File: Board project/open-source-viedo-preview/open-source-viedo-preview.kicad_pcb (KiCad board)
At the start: 4 copper layers, 99.6 x 55.4 mm, 98 parts, among them J1 Conn_02x07_Odd_Even, J10 Conn_01x22_Female, J11 HDMI_A_1.4, J12 HDMI_A_1.4, J13 Screw_Terminal_01x02, J14 AMP171826-4, J15 10018783-11200TLF, J16 USB_OTG, J2 Conn_01x03, J3 Conn_01x03, J4 7499110124, J5 Micro_SD_Card_Det, J6 Conn_02x20_Odd_Even, J7 Conn_01x22_Female, J8 Conn_01x22_Female, J9 Conn_01x22_Female, Q1 DMP3013SFV-7, Q2 BSS138PW, U1 74LVC1G07, U131 TPD4EUSB30, U132 TPD4EUSB30, U2 74LVC1G07, U3 AP64501SP-13, U4 AP64501SP-13, U5 TPD2E009DBZR, U6 TPD2E009DBZR

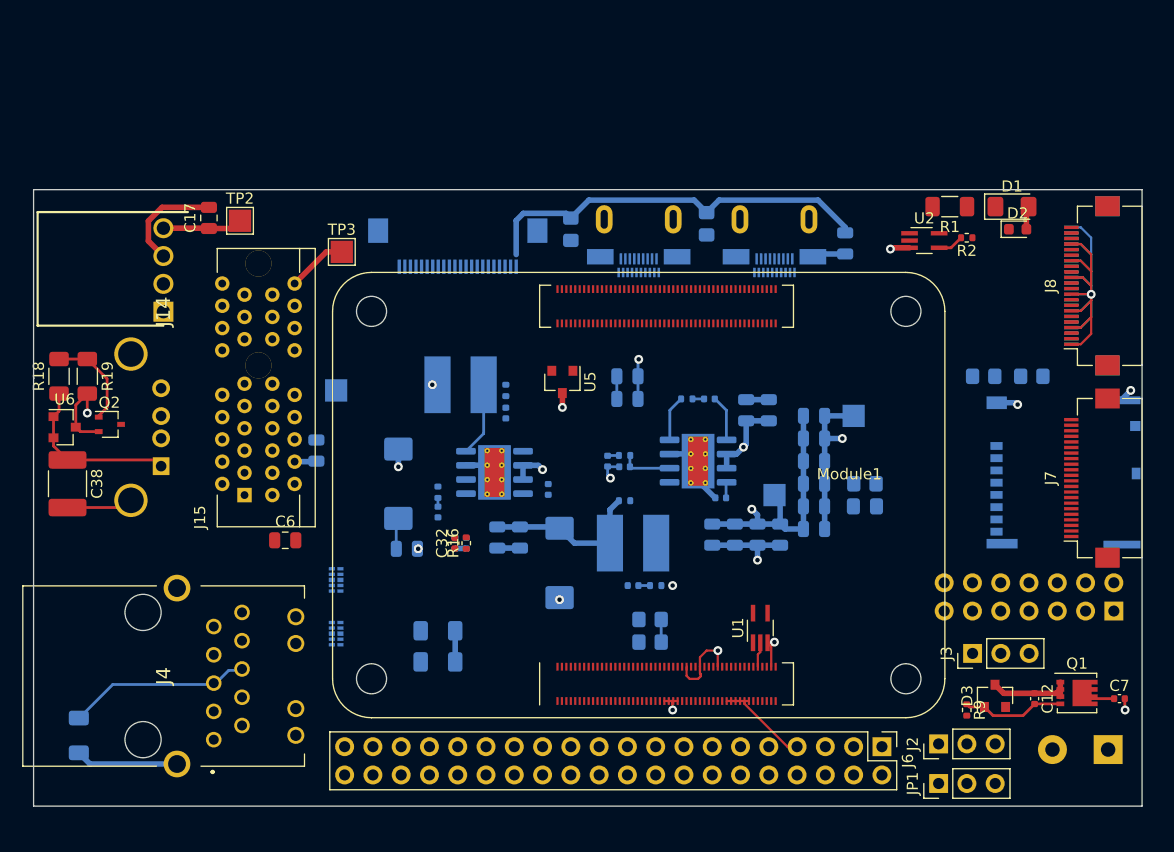
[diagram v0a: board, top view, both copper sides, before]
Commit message: Elements new placement
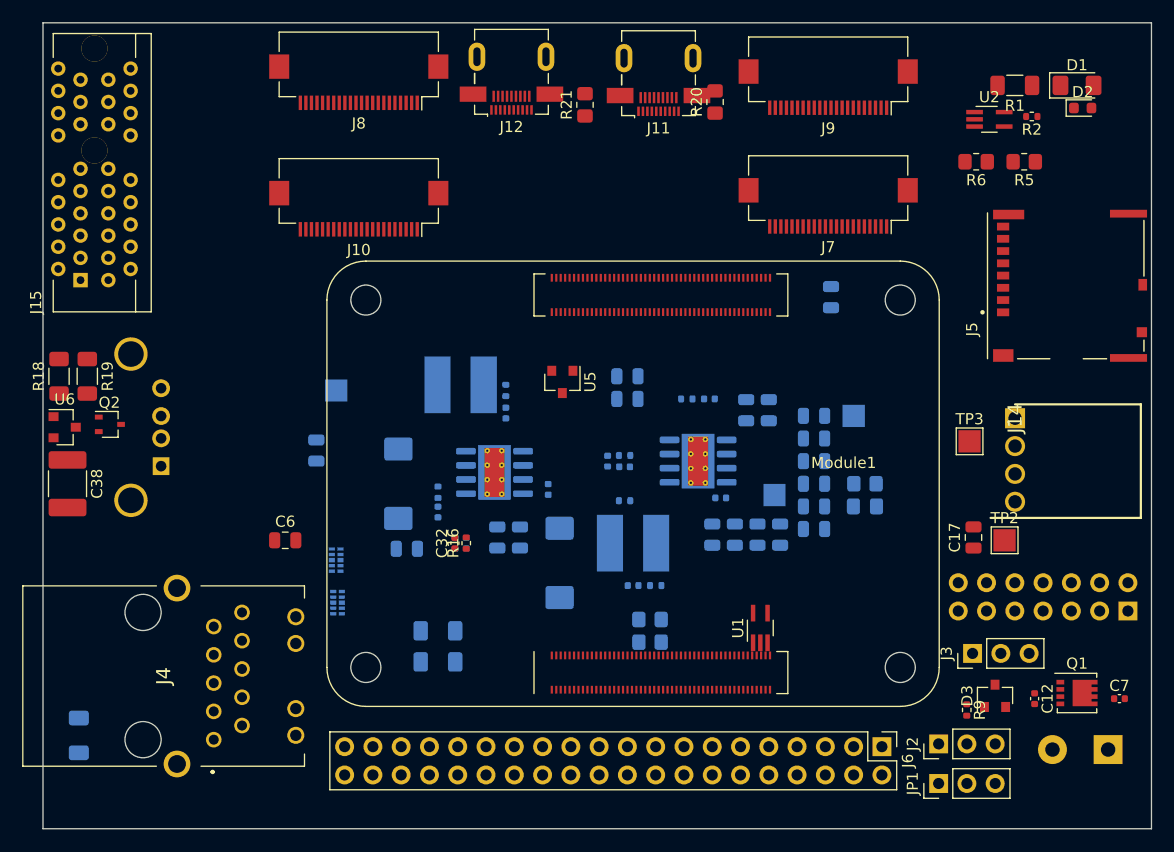
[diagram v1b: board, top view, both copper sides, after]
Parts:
- J10, J11, J12, J5, J9, R20, R21, R5, R6: moved to F.Cu
- moved J14 77.1 mm to (189.8, 55.1), turned to -90 degrees
- moved C17 74.4 mm to (186.0, 65.8)
- moved TP2 74.4 mm to (188.8, 66.0)
- moved J8 68.3 mm to (130.8, 24.9), turned to 180 degrees
- moved TP3 58.9 mm to (185.7, 57.1)
- moved J7 34.0 mm to (173.0, 36.0), turned to 180 degrees
- moved J9 29.7 mm to (173.0, 25.3), turned to 180 degrees
- moved J12 27.8 mm to (144.5, 22.6), turned to 180 degrees
- moved J15 24.3 mm to (105.8, 42.7)
- moved R6 19.9 mm to (186.3, 32.0), turned to 180 degrees
- moved R5 19.6 mm to (190.6, 32.0), turned to 180 degrees
- moved R20 17.3 mm to (162.8, 26.7), turned to 90 degrees
- moved J5 16.8 mm to (194.3, 43.2), turned to 90 degrees
- moved R21 15.3 mm to (151.1, 26.9), turned to 90 degrees
- moved J11 14.6 mm to (157.7, 22.7), turned to 180 degrees
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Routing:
- net GND: track 148.8 -> 0.00 mm, vias 18 -> 0
- net +12V: track 120.0 -> 0.00 mm, vias 3 -> 0
- net +3V3: track 71.7 -> 0.00 mm
- net /pcie/+3.3v: track 38.0 -> 0.00 mm, vias 1 -> 0
- net Net-(C2-Pad1): track 16.3 -> 0.00 mm
- net Net-(C38-Pad1): track 15.3 -> 0.00 mm
- net Net-(C12-Pad2): track 9.26 -> 0.00 mm
- net Net-(Q2-Pad1): track 8.80 -> 0.00 mm
- net Net-(L2-Pad1): track 6.63 -> 0.00 mm
- net Net-(C13-Pad1): track 4.64 -> 0.00 mm
- net Net-(L1-Pad1): track 4.23 -> 0.00 mm
- net Net-(C10-Pad2): track 3.98 -> 0.00 mm
- net Net-(C7-Pad1): track 3.09 -> 0.00 mm
- net Net-(R2-Pad2): track 2.34 -> 0.00 mm
- net /video_previewGPIO/RUN_PG: track 2.24 -> 0.00 mm
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- removed copper zone on In1.Cu, net GND
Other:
- board size 99.6 x 55.4 mm -> 99.6 x 72.4 mm
